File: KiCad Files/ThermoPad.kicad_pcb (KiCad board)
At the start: 2 copper layers, 81.5 x 28 mm, 14 parts, among them J1 Conn_02x01, SW1 SW_Push, U1 XIAO-RP2040-DIP, U2 DM-OLED096-636, U3 SHT30-DIS-B2.5KS

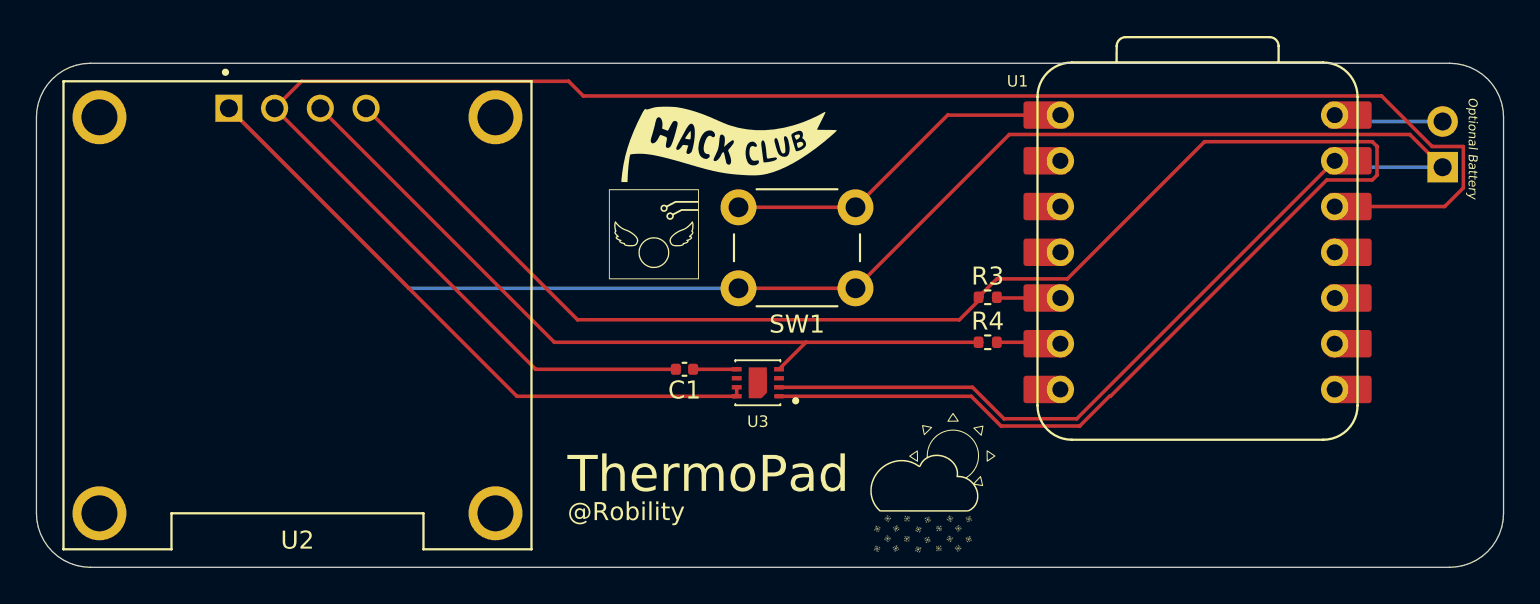
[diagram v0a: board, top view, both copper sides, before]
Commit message: Update Pull-Up Resistors
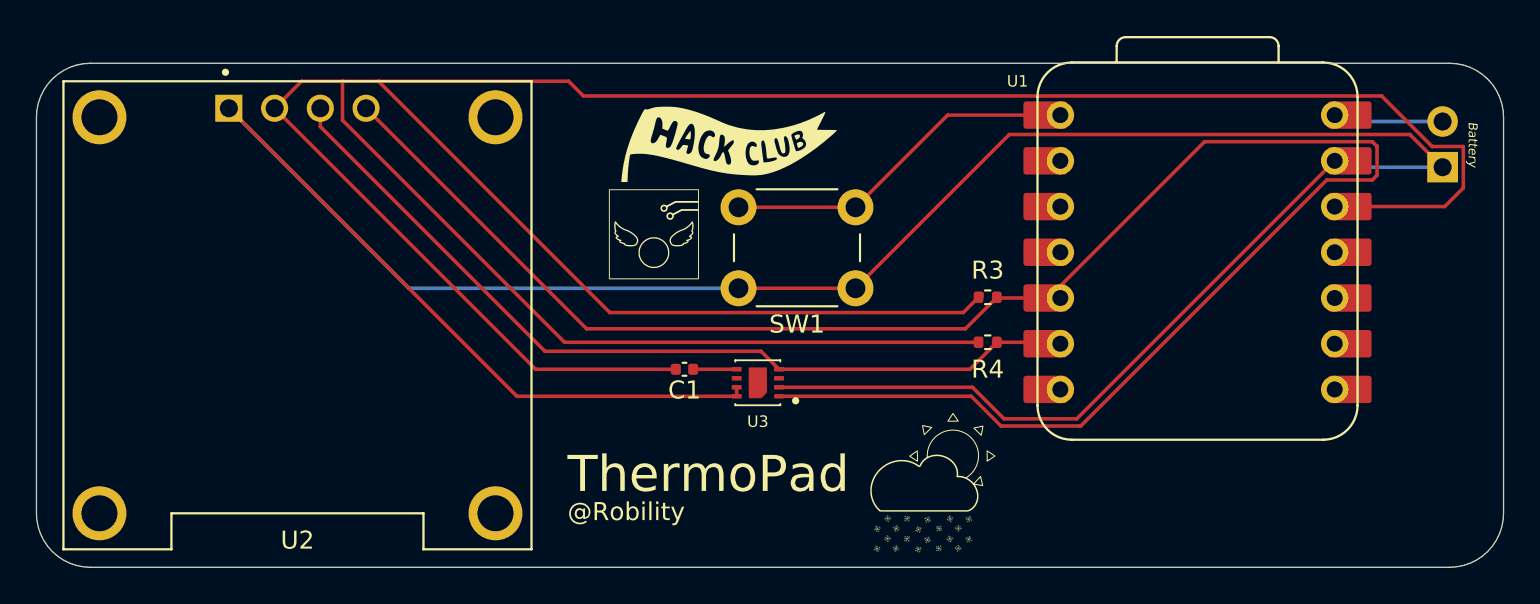
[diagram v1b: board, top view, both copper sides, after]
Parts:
- turned R3 to 180 degrees
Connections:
- R3 pad 2: Net-(U1-GPIO6/SDA) -> +3.3V
- R4 pad 1: SCL -> +3.3V
- R4 pad 2: Net-(U1-GPIO7/SCL) -> SCL
- U1 pad 5: Net-(U1-GPIO6/SDA) -> SDA
- U1 pad 6: Net-(U1-GPIO7/SCL) -> SCL
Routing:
- net +3.3V: track 106.3 -> 188.1 mm
- net SCL: track 44.3 -> 47.7 mm
- net Net-(U1-GPIO7/SCL): track 2.91 -> 0.00 mm
- net Net-(U1-GPIO6/SDA): track 2.90 -> 0.00 mm
- net SDA: track 106.6 -> 107.5 mm
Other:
- board text added: "Battery"
- board text removed: "Optional Battery"
